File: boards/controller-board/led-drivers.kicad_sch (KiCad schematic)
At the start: 169 parts, among them IC10 A6214KLKTR-T, IC11 A6214KLKTR-T, IC12 A6214KLKTR-T, IC13 A6214KLKTR-T, IC2 A6214KLKTR-T, IC3 A6214KLKTR-T, IC4 A6214KLKTR-T, IC5 A6214KLKTR-T, IC6 A6214KLKTR-T, IC7 A6214KLKTR-T, IC8 A6214KLKTR-T, IC9 A6214KLKTR-T

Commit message: minor changes to schematic, pcb, and BOM
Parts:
- C41, C42, C43, C50, C51, C57, C58, C59, C60, C61, C62, C64: DPN 587-3248-1-ND -> 1292-1206B106K250CT-ND; MFR Taiyo Yuden -> Walsin Technology Corporation; MPN UMK316BBJ106ML-T -> 1206B106K250CT
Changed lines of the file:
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@@
 			)
 		)
-		(property "DPN" "587-3248-1-ND"
+		(property "DPN" "1292-1206B106K250CT-ND"
 			(at 407.67 142.24 0)
 			(effects
@@
 			)
 		)
-		(property "MFR" "Taiyo Yuden"
+		(property "MFR" "Walsin Technology Corporation"
 			(at 407.67 142.24 0)
 			(effects
@@
 			)
 		)
-		(property "MPN" "UMK316BBJ106ML-T"
+		(property "MPN" "1206B106K250CT"
 			(at 407.67 142.24 0)
 			(effects
@@
 			)
 		)
-		(property "DPN" "587-3248-1-ND"
+		(property "DPN" "1292-1206B106K250CT-ND"
 			(at 86.36 139.7 0)
 			(effects
@@
 			)
 		)
-		(property "MFR" "Taiyo Yuden"
+		(property "MFR" "Walsin Technology Corporation"
 			(at 86.36 139.7 0)
 			(effects
@@
 			)
 		)
-		(property "MPN" "UMK316BBJ106ML-T"
+		(property "MPN" "1206B106K250CT"
 			(at 86.36 139.7 0)
 			(effects
@@
 			)
 		)
-		(property "DPN" "587-3248-1-ND"
+		(property "DPN" "1292-1206B106K250CT-ND"
 			(at 245.11 209.55 0)
 			(effects
@@
 			)
 		)
-		(property "MFR" "Taiyo Yuden"
+		(property "MFR" "Walsin Technology Corporation"
 			(at 245.11 209.55 0)
 			(effects
@@
 			)
 		)
-		(property "MPN" "UMK316BBJ106ML-T"
+		(property "MPN" "1206B106K250CT"
 			(at 245.11 209.55 0)
 			(effects
@@
 			)
 		)
-		(property "DPN" "587-3248-1-ND"
+		(property "DPN" "1292-1206B106K250CT-ND"
 			(at 245.11 144.78 0)
 			(effects
@@
 			)
 		)
-		(property "MFR" "Taiyo Yuden"
+		(property "MFR" "Walsin Technology Corporation"
 			(at 245.11 144.78 0)
 			(effects
@@
 			)
 		)
-		(property "MPN" "UMK316BBJ106ML-T"
+		(property "MPN" "1206B106K250CT"
 			(at 245.11 144.78 0)
 			(effects
@@
 			)
 		)
-		(property "DPN" "587-3248-1-ND"
+		(property "DPN" "1292-1206B106K250CT-ND"
 			(at 407.67 204.47 0)
 			(effects
@@
 			)
 		)
-		(property "MFR" "Taiyo Yuden"
+		(property "MFR" "Walsin Technology Corporation"
 			(at 407.67 204.47 0)
 			(effects
@@
 			)
 		)
-		(property "MPN" "UMK316BBJ106ML-T"
+		(property "MPN" "1206B106K250CT"
 			(at 407.67 204.47 0)
 			(effects
@@
 			)
 		)
-		(property "DPN" "587-3248-1-ND"
+		(property "DPN" "1292-1206B106K250CT-ND"
 			(at 245.11 76.2 0)
 			(effects
@@
 			)
 		)
-		(property "MFR" "Taiyo Yuden"
+		(property "MFR" "Walsin Technology Corporation"
 			(at 245.11 76.2 0)
 			(effects
@@
 			)
 		)
-		(property "MPN" "UMK316BBJ106ML-T"
+		(property "MPN" "1206B106K250CT"
 			(at 245.11 76.2 0)
 			(effects
@@
 			)
 		)
-		(property "DPN" "587-3248-1-ND"
+		(property "DPN" "1292-1206B106K250CT-ND"
 			(at 407.67 77.47 0)
 			(effects
@@
 			)
 		)
-		(property "MFR" "Taiyo Yuden"
+		(property "MFR" "Walsin Technology Corporation"
 			(at 407.67 77.47 0)
 			(effects
@@
 			)
 		)
-		(property "MPN" "UMK316BBJ106ML-T"
+		(property "MPN" "1206B106K250CT"
 			(at 407.67 77.47 0)
 			(effects
@@
 			)
 		)
-		(property "DPN" "587-3248-1-ND"
+		(property "DPN" "1292-1206B106K250CT-ND"
 			(at 245.11 271.78 0)
 			(effects
@@
 			)
 		)
-		(property "MFR" "Taiyo Yuden"
+		(property "MFR" "Walsin Technology Corporation"
 			(at 245.11 271.78 0)
 			(effects
@@
 			)
 		)
-		(property "MPN" "UMK316BBJ106ML-T"
+		(property "MPN" "1206B106K250CT"
 			(at 245.11 271.78 0)
 			(effects
@@
 			)
 		)
-		(property "DPN" "587-3248-1-ND"
+		(property "DPN" "1292-1206B106K250CT-ND"
 			(at 86.36 203.2 0)
 			(effects
@@
 			)
 		)
-		(property "MFR" "Taiyo Yuden"
+		(property "MFR" "Walsin Technology Corporation"
 			(at 86.36 203.2 0)
 			(effects
@@
 			)
 		)
-		(property "MPN" "UMK316BBJ106ML-T"
+		(property "MPN" "1206B106K250CT"
 			(at 86.36 203.2 0)
 			(effects
@@
 			)
 		)
-		(property "DPN" "587-3248-1-ND"
+		(property "DPN" "1292-1206B106K250CT-ND"
 			(at 407.67 267.97 0)
 			(effects
@@
 			)
 		)
-		(property "MFR" "Taiyo Yuden"
+		(property "MFR" "Walsin Technology Corporation"
 			(at 407.67 267.97 0)
 			(effects
@@
 			)
 		)
-		(property "MPN" "UMK316BBJ106ML-T"
+		(property "MPN" "1206B106K250CT"
 			(at 407.67 267.97 0)
 			(effects
@@
 			)
 		)
-		(property "DPN" "587-3248-1-ND"
+		(property "DPN" "1292-1206B106K250CT-ND"
 			(at 86.36 265.43 0)
 			(effects
@@
 			)
 		)
-		(property "MFR" "Taiyo Yuden"
+		(property "MFR" "Walsin Technology Corporation"
 			(at 86.36 265.43 0)
 			(effects
@@
 			)
 		)
-		(property "MPN" "UMK316BBJ106ML-T"
+		(property "MPN" "1206B106K250CT"
 			(at 86.36 265.43 0)
 			(effects
@@
 			)
 		)
-		(property "DPN" "587-3248-1-ND"
+		(property "DPN" "1292-1206B106K250CT-ND"
 			(at 86.36 74.93 0)
 			(effects
@@
 			)
 		)
-		(property "MFR" "Taiyo Yuden"
+		(property "MFR" "Walsin Technology Corporation"
 			(at 86.36 74.93 0)
 			(effects
@@
 			)
 		)
-		(property "MPN" "UMK316BBJ106ML-T"
+		(property "MPN" "1206B106K250CT"
 			(at 86.36 74.93 0)
 			(effects

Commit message: removed 100k pull-down resistors from LED drivers and added a 100k resistor to each output of DAC, other misc schematic and pcb changes
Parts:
- removed R48, R49, R50, R51, R52, R53, R54, R55, R56, R57, R58, R59: 100k, oresat-passives:0603-C, symbol Device:R_Small_US
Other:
- note removed: "check that 10uF bypass cap drivers works (we have some on hand, ordering from digikey requires 2000+ units)"

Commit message: minor changes
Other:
- note removed: "add 100k pull-down resistor for adim pins"
- note removed: "check buck conv. diode. better alternative (smaller voltage/smaller footprint)?"
- moved on the sheet: C20, C21, C22, C23, C24, C25, C26, C27, C28, C29, C30, C31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

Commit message: Andrew polishing: arbitrary schematic changes to make it pretty, and then updating zones to have fillets and smaller widths, and a billion ground vias.
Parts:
- R17, R6: value .576 -> .576
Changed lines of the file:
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@@
 			)
 		)
-		(property "Value" ".576	"
+		(property "Value" ".576"
 			(at 322.072 214.6301 0)
 			(effects
@@
 			)
 		)
-		(property "Value" ".576	"
+		(property "Value" ".576"
 			(at 163.322 87.6301 0)
 			(effects

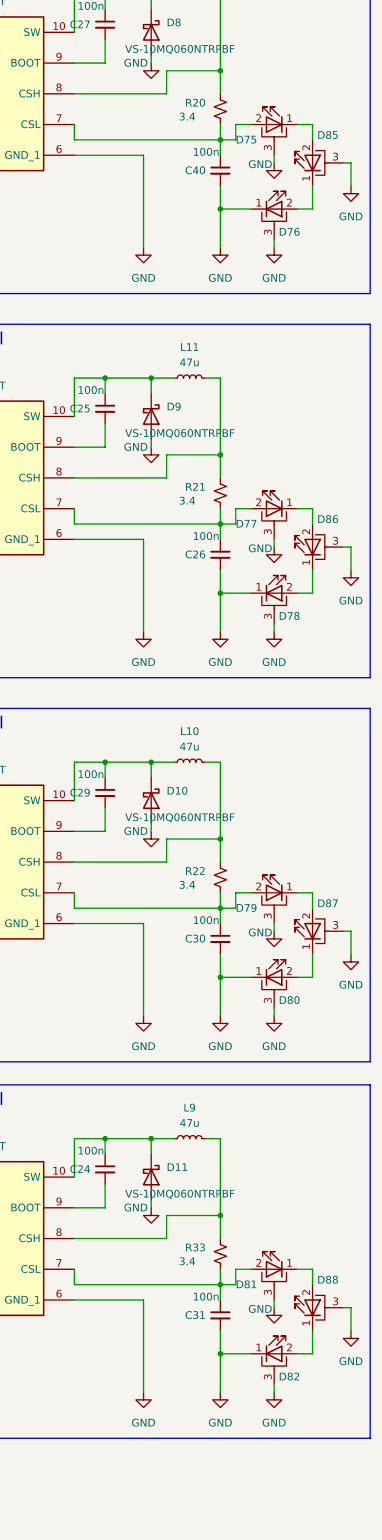
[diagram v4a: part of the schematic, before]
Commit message: replaced led footprints for UV lights
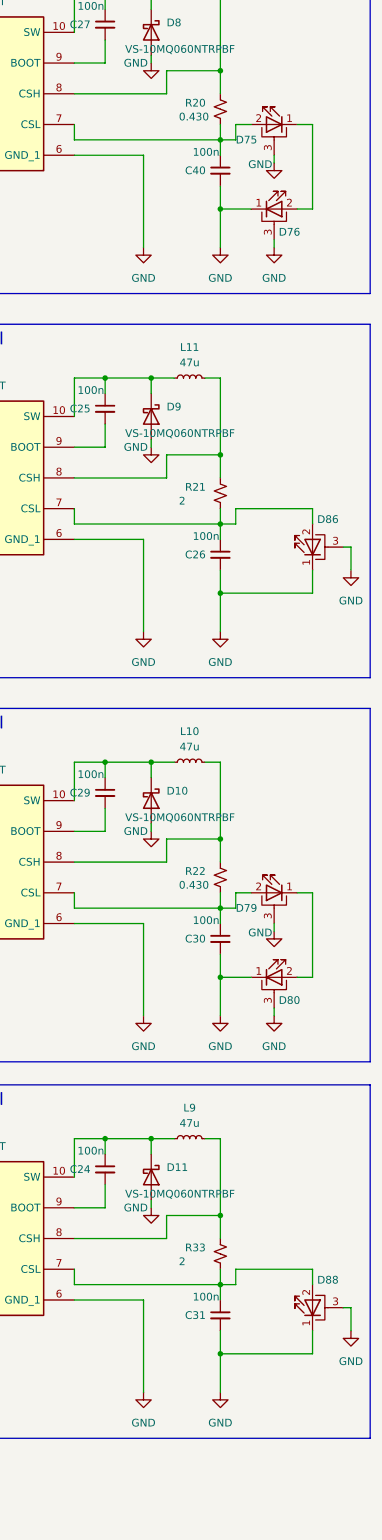
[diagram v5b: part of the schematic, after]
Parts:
- removed D77, D78, D81, D82, D85, D87: 153283367A212, oresat-diodes:Cree-LED, symbol Device:LED_Pad
- D75, D76, D79, D80: value 153283367A212 -> UVA LED; footprint oresat-diodes:Cree-LED -> oresat-diodes:LED-Everlight-1414-UVA; DPN 732-153283367A212CT-ND -> 1080-1629-1-ND; MFR Würth Elektronik -> Everlight Electronics Co Ltd; MPN 153283367A212 -> ELUA3535OGB-P6070U23240500-VD1M
- D86: value 153283367A212 -> UVC LED; DPN 732-153283367A212CT-ND -> 1080-ELUC3535NUB-P7085Q15070100-S22QCT-ND; MFR Würth Elektronik -> Everlight Electronics Co Ltd; MPN 153283367A212 -> ELUC3535NUB-P7085Q15070100-S22Q
- D88: value 153283367A212 -> UVC LED; footprint oresat-diodes:Cree-LED -> oresat-diodes:LED-Everlight-1414-UVC; DPN 732-153283367A212CT-ND -> 1080-ELUC3535NUB-P7085Q15070100-S22QCT-ND; MFR Würth Elektronik -> Everlight Electronics Co Ltd; MPN 153283367A212 -> ELUC3535NUB-P7085Q15070100-S22Q
- R20: value 3.4 -> 0.430; DPN 541-3.40HHCT-ND -> P17399CT-ND; Distributor DigiKey -> ERJ-3BQFR43V; MFR Vishay Dale -> Panasonic Electronic Components; MPN CRCW06033R40FKEA -> ERJ-3BQFR43V
- R21, R33: value 3.4 -> 2; DPN 541-3.40HHCT-ND -> 311-2.00HRCT-ND; MFR Vishay Dale -> YAGEO; MPN CRCW06033R40FKEA -> RC0603FR-072RL
- R22: value 3.4 -> 0.430; DPN 541-3.40HHCT-ND -> P17399CT-ND; MFR Vishay Dale -> Panasonic Electronic Components; MPN CRCW06033R40FKEA -> ERJ-3BQFR43V
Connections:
- net GND: now also D86.1 (K), D88.1 (K)
- net at D75.1 (K): now also D76.2 (A)
- net at C26.1, IC11.7 (CSL), R21.2: now also D86.2 (A)
- net at C31.1, IC13.7 (CSL), R33.2: now also D88.2 (A)
- net at D80.2 (A): now also D79.1 (K)
